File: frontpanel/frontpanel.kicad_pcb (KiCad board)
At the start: 2 copper layers, 80.9 x 128.5 mm, 12 parts

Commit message: finished routing
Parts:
- added REF**: SONGHUEI_R0904N_MountingHole_6.3mm_Silkscreen+-, CHAIR:SONGHUEI_R0904N_NoHole_Silkscreen-+, F.Cu at (79.3, 91.0)
- moved REF** 36.9 mm to (104.7, 61.5)
- moved REF** 31.5 mm to (130.2, 120.5)
- moved REF** 31.3 mm to (104.8, 91.0)
- moved REF** 24.5 mm to (104.8, 120.3)
- moved REF** 24.1 mm to (79.3, 120.3)
- moved G*** 24.0 mm to (104.3, 181.8)
- moved REF** 22.1 mm to (130.1, 61.5)
- moved REF** 17.8 mm to (79.4, 61.5)
- moved REF** 11.3 mm to (130.2, 91.0)
- moved H2 10.1 mm to (125.2, 36.8)
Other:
- board size 80.9 x 128.5 mm -> 70.8 x 128.5 mm
- board text removed: "Happiness"
- board text removed: "JLCJLCJLCJLC"

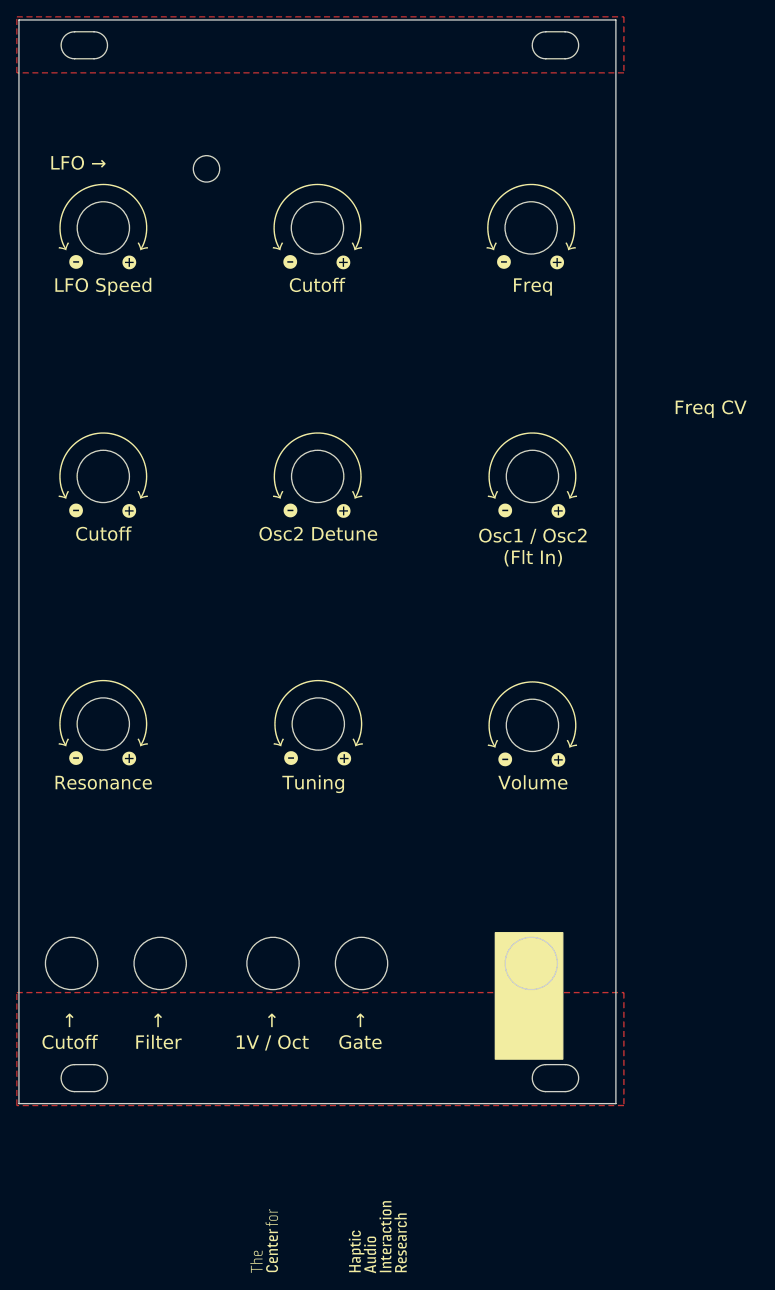
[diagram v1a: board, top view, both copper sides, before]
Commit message: updated frontpanel
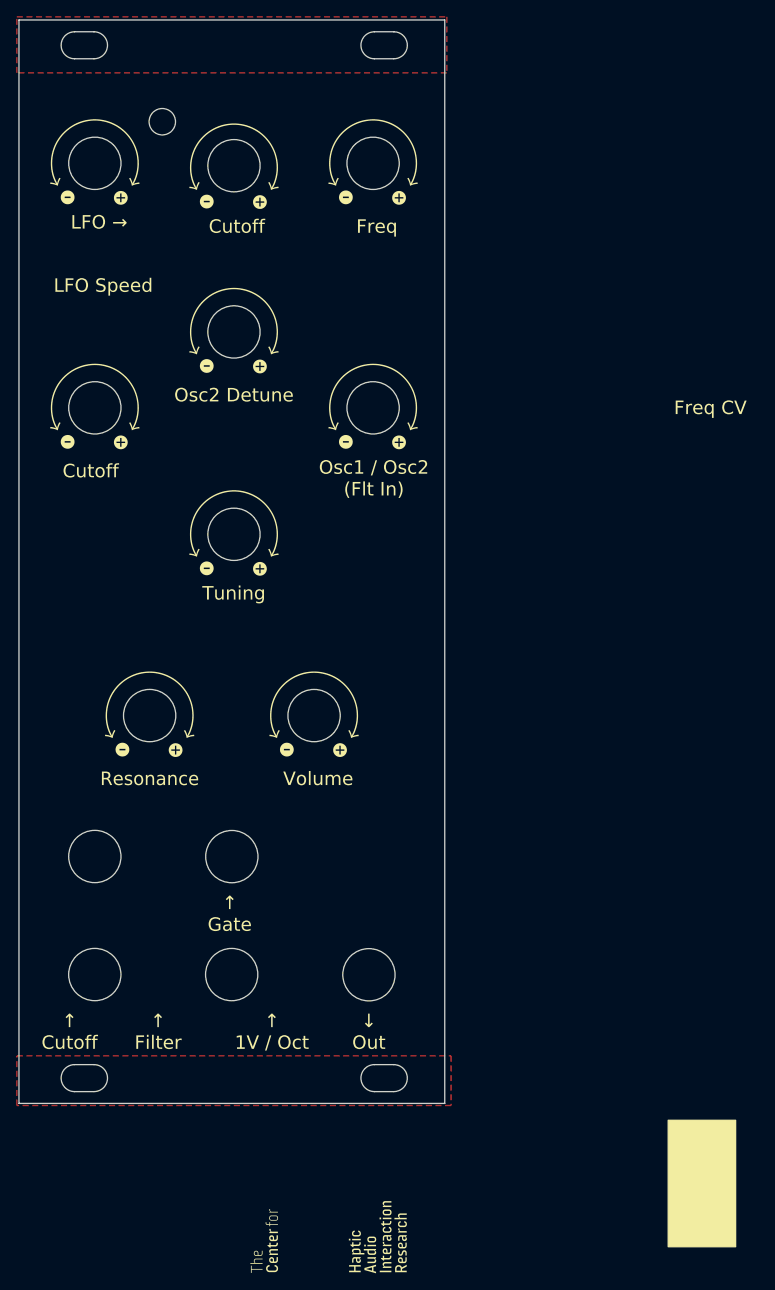
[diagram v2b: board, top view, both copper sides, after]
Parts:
- moved REF** 25.9 mm to (104.3, 119.3)
- moved REF** 24.6 mm to (94.8, 97.8)
- moved REF** 20.6 mm to (111.3, 82.8)
- moved H2 20.3 mm to (104.9, 36.8)
- moved REF** 20.3 mm to (111.3, 53.8)
- moved REF** 19.8 mm to (94.8, 73.8)
- moved REF** 12.2 mm to (94.8, 54.3)
- moved REF** 8.20 mm to (78.3, 82.8)
- moved REF** 7.73 mm to (78.3, 53.8)
- moved REF** 5.59 mm to (84.8, 119.3)
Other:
- board size 70.8 x 128.5 mm -> 50.5 x 128.5 mm
